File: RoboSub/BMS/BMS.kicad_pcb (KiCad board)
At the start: 2 copper layers, 72.2 x 72.2 mm, 36 parts, among them J1 CAN, J2 CAN, J3 DuraClik, J4 XT90, J5 XT90, J6 SWD_UART, J7 ExtPwrSw, K1 A3_Relay, Q1 PMV28ENEA, SW2 DBG2, SW3 DBG1, SW4 RST, U1 VXO7803, U2 TCAN330G, U3 STM32G0B1KxTxN, U4 CZ3AG7_HalEfSens

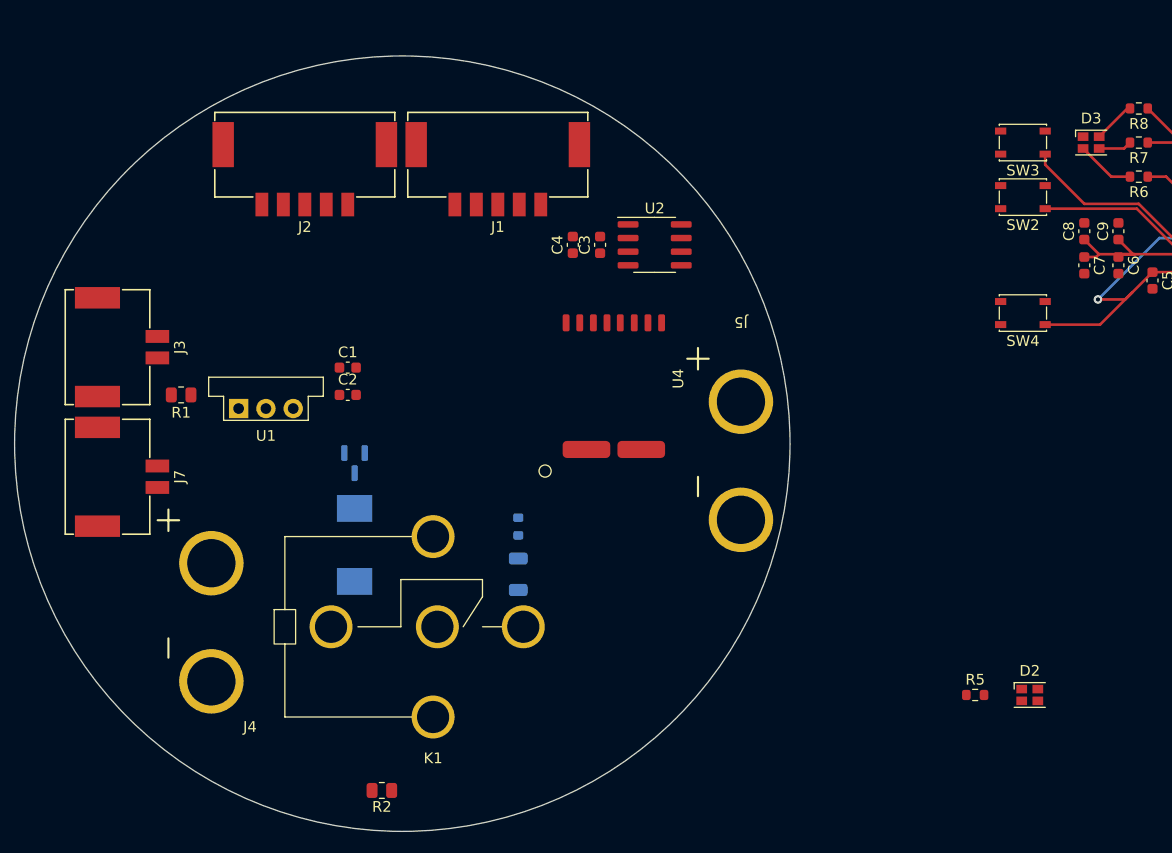
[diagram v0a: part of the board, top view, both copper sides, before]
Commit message: cleaned up schematic
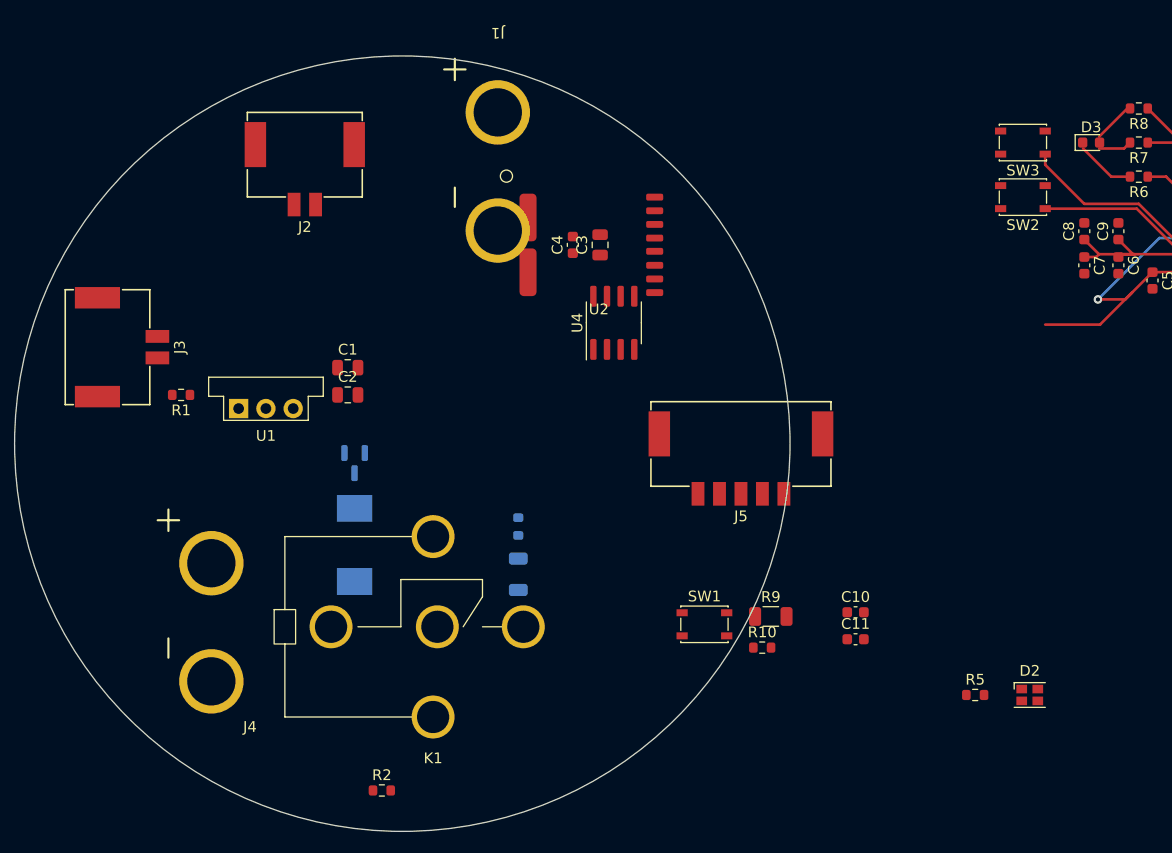
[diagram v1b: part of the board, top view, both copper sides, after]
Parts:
- removed J7: ExtPwrSw, extraparts:Molex_DuraClik_Vert_2pin
- removed SW4: RST, Button_Switch_SMD:SW_SPST_PTS810
- added C10: 100n, Capacitor_SMD:C_0603_1608Metric, F.Cu at (93.0, 68.5)
- added C11: 4.7u, Capacitor_SMD:C_0603_1608Metric, F.Cu at (93.0, 71.0)
- added R10: 120, Resistor_SMD:R_0603_1608Metric, F.Cu at (84.3, 71.8)
- added R9: 1k, Resistor_SMD:R_1206_3216Metric, F.Cu at (85.1, 68.9)
- added SW1: DBG2, Button_Switch_SMD:SW_SPST_PTS810, F.Cu at (78.9, 69.6)
- C1: value 4.7uF -> 10u; footprint Capacitor_SMD:C_0603_1608Metric -> Capacitor_SMD:C_0805_2012Metric
- C2: value 10uF -> 10u; footprint Capacitor_SMD:C_0603_1608Metric -> Capacitor_SMD:C_0805_2012Metric
- C3: value 100n -> 10u; footprint Capacitor_SMD:C_0603_1608Metric -> Capacitor_SMD:C_0805_2012Metric
- C4: value 4.7u -> 100n
- D2: value LED -> LED_ARGB
- D3: value LED_ARGB -> LED; footprint LED_SMD:LED_Cree-PLCC4_2x2mm_CW -> LED_SMD:LED_0603_1608Metric
- J1: value CAN -> battery; footprint extraparts:Molex_DuraClik_Vert_5pin -> BMS_Library:Conn_XT90
- J2: value CAN -> temp; footprint extraparts:Molex_DuraClik_Vert_5pin -> extraparts:Molex_DuraClik_Vert_2pin
- J3: value DuraClik -> ExtPwrSw
- J4: value XT90 -> output
- J5: value XT90 -> CAN; footprint BMS_Library:Conn_XT90 -> extraparts:Molex_DuraClik_Vert_5pin
- K1: value A3_Relay -> A31ASQ12VDC2R
- R1: footprint Resistor_SMD:R_0805_2012Metric -> Resistor_SMD:R_0603_1608Metric
- R2: value 10 -> 10k; footprint Resistor_SMD:R_0805_2012Metric -> Resistor_SMD:R_0603_1608Metric
- R3: value 4k -> 10
- R4: value 1k -> 100k
- R5: value 250 -> 10k
- SW2: value DBG2 -> DBG1
- SW3: value DBG1 -> RST
- U2: value TCAN330G -> CZ3A07; footprint Package_SO:SOIC-8_3.9x4.9mm_P1.27mm -> BMS_Library:CZ3AG7_HalEfSens
- U4: value CZ3AG7_HalEfSens -> TCAN330G; footprint BMS_Library:CZ3AG7_HalEfSens -> Package_SO:SOIC-8_3.9x4.9mm_P1.27mm
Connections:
- C1 pad 1: Net-(C1-Pad1) -> GND
- C1 pad 2: GND -> Net-(C1-Pad2)
- D2 pad 1: GND -> +3V3
- D2 pad 2: Net-(D2-Pad2) -> /R
- D2 pad 3: (no net) -> /G
- D2 pad 4: (no net) -> /B
- D3 pad 1: +3V3 -> GND
- D3 pad 2: /R -> Net-(D3-Pad2)
- J1 pad 1: Net-(J1-Pad1) -> GND
- J1 pad 2: Net-(J1-Pad2) -> +BATT
- J2 pad 1: Net-(J1-Pad1) -> GND
- J2 pad 2: Net-(J1-Pad2) -> /T_sense
- J3 pad 1: /T_sense -> Net-(C1-Pad2)
- J3 pad 2: GND -> +BATT
- J4 pad 1: +BATT -> GND
- J4 pad 2: GND -> VBUS
- J5 pad 1: /V_out -> VBUS
- J5 pad 2: GND -> /PCC_3V3
- K1 pad 85: Net-(D1-Pad2) -> +BATT
- K1 pad 86: Net-(D1-Pad1) -> Net-(D1-Pad2)
- K1 pad 87: /IP -> /VRAW
- Q1 pad 1: /MOSFET1 -> /enable
- Q1 pad 3: Net-(D1-Pad1) -> Net-(Q1-Pad3)
- R2 pad 1: +BATT -> GND
- R2 pad 2: Net-(D1-Pad2) -> /enable
- R3 pad 1: /V_sense -> Net-(Q1-Pad3)
- R3 pad 2: /IP -> Net-(D1-Pad2)
- R4 pad 1: /V_sense -> /VRAW
- R4 pad 2: GND -> /V_sense
- R5 pad 1: Net-(D2-Pad2) -> /V_sense
- R5 pad 2: /V_out -> GND
- SW2 pad 1: /DBG2 -> /DBG1
- SW3 pad 1: /DBG1 -> /RST
- U1 pad 1: Net-(C1-Pad1) -> Net-(C1-Pad2)
- U2 pad 1: /CAN_TX -> /VRAW
- U2 pad 5: unconnected-(U2-Pad5) -> VBUS
- U3 pad 11: /MOSFET1 -> /enable
- U4 pad 1: /IP -> /CAN_TX
- U4 pad 5: /V_out -> unconnected-(U4-Pad5)
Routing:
- net /RST: track 47.2 -> 64.4 mm
- net /DBG2: track 14.9 -> 0.00 mm
- net /R: track 3.96 -> 7.06 mm
- net /G: track 3.10 -> 0.00 mm
- net /DBG1: track 17.2 -> 14.9 mm

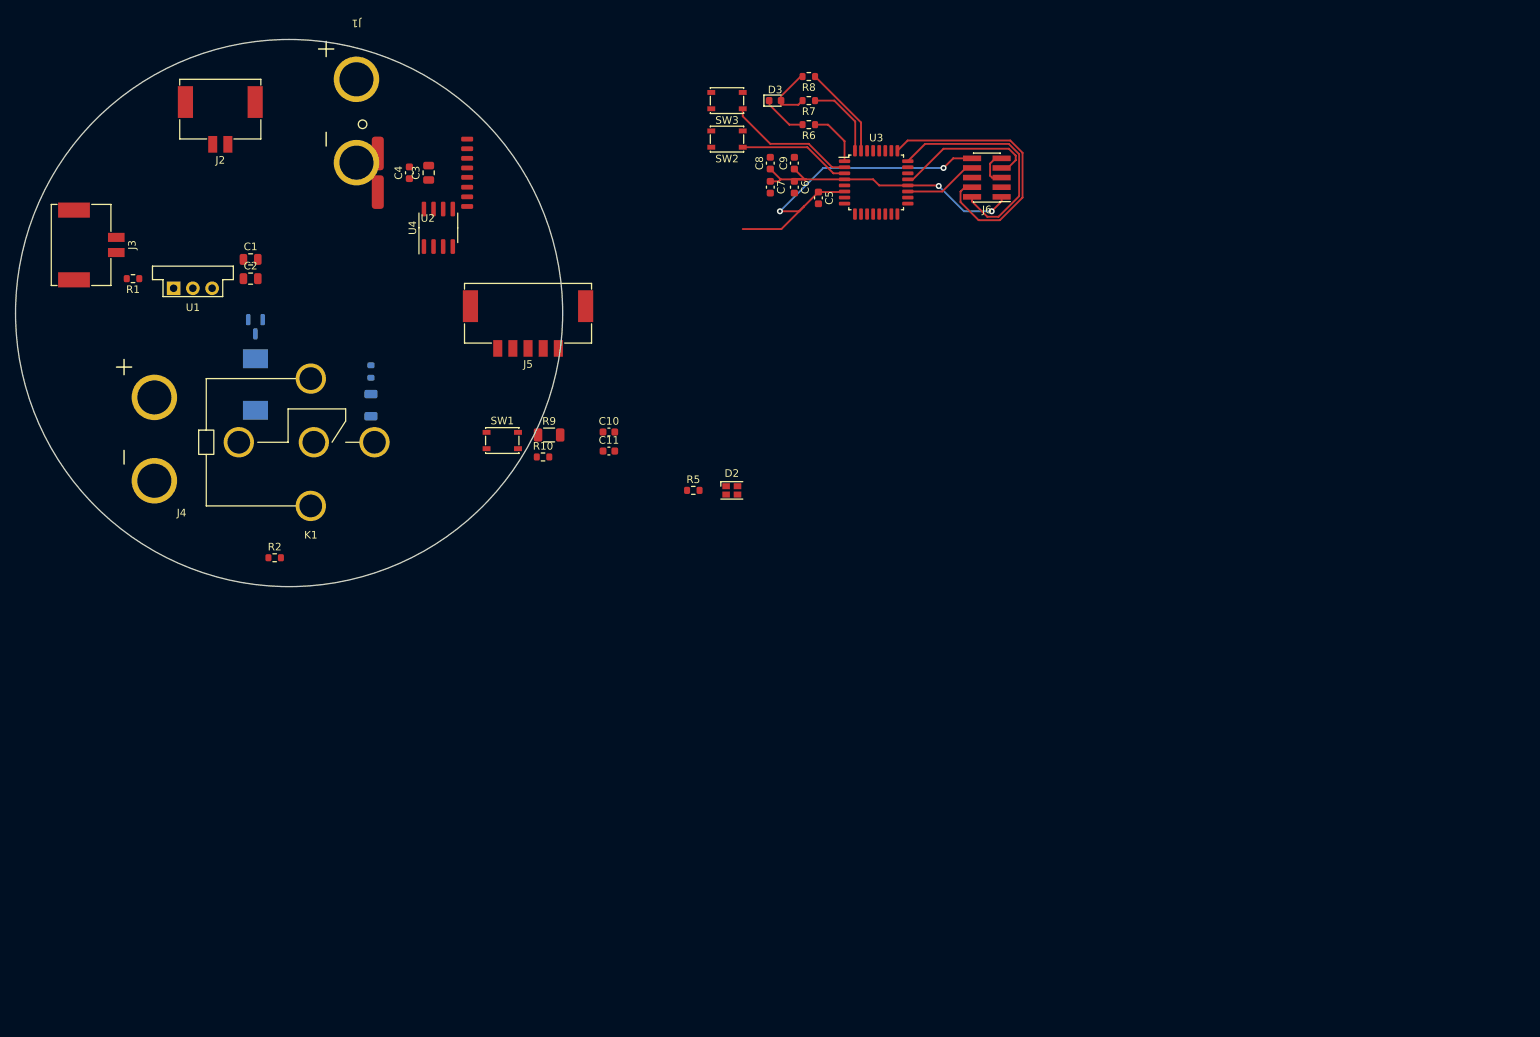
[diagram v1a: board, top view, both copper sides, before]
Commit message: PCC added to BMS. TODO: change TVS diode.
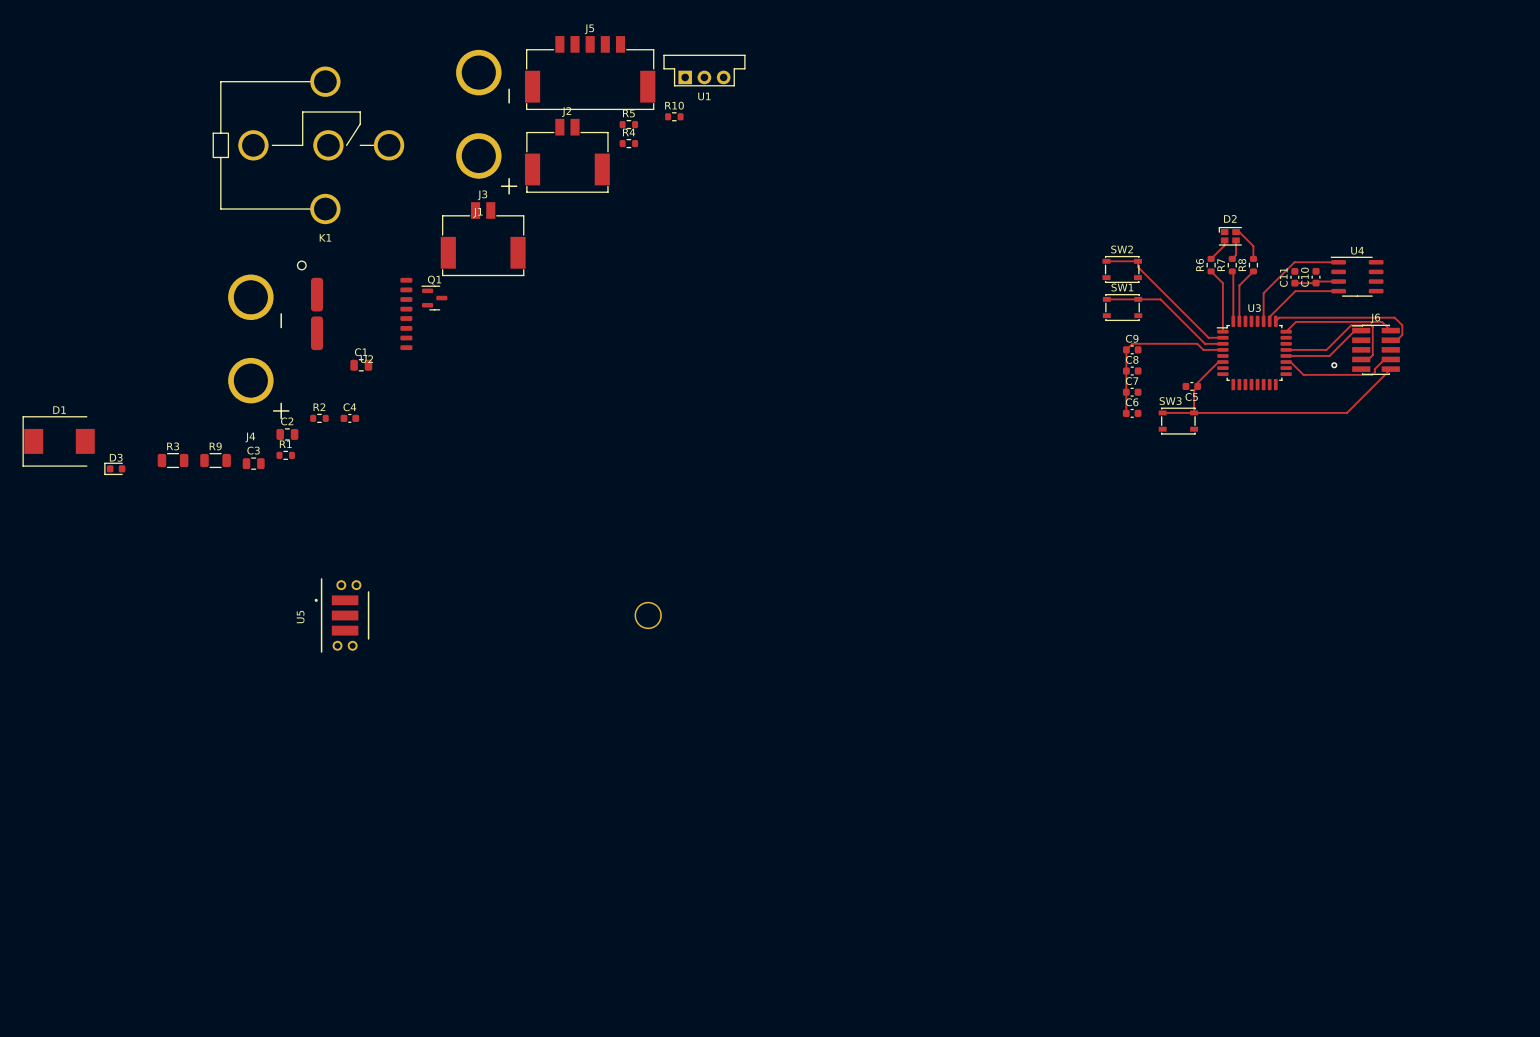
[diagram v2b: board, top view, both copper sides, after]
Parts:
- added U5: PCC, BMS_Library:PCC_footprint, F.Cu at (58.2, 92.7)
- D1: value TVS_Diode -> SMCJ13A_TVS; moved to F.Cu
- K1: value A31ASQ12VDC2R -> A31CSP12VDC2D
- Q1, R3, R4: moved to F.Cu
- moved U4 121.4 mm to (191.8, 48.0), turned to 0 degrees
- moved D3 99.6 mm to (28.0, 73.4)
- moved C10 95.5 mm to (186.3, 48.1), turned to 90 degrees
- moved C11 93.4 mm to (183.5, 48.1), turned to 90 degrees
- moved SW1 83.7 mm to (160.8, 52.1)
- moved D2 73.8 mm to (175.0, 42.7)
- moved SW3 73.0 mm to (168.1, 67.1), turned to 0 degrees
- moved U1 73.0 mm to (103.1, 21.7)
- moved R8 63.7 mm to (178.1, 46.5), turned to 90 degrees
- moved R7 60.0 mm to (175.3, 46.5), turned to 90 degrees
- moved J3 57.1 mm to (76.4, 47.8), turned to 0 degrees
- moved R6 56.2 mm to (172.5, 46.5), turned to 90 degrees
- moved J6 56.2 mm to (194.2, 57.7), turned to 0 degrees
- moved C5 55.2 mm to (169.9, 62.5), turned to 180 degrees
- moved C8 55.1 mm to (162.1, 60.5), turned to 0 degrees
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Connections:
- D1 pad 1: Net-(D1-Pad1) -> +BATT
- K1 pad 87a: (no net) -> unconnected-(K1-Pad87a)
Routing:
- net /RST: track 64.4 -> 41.1 mm, vias 2 -> 0
- net /DBG2: track 0.00 -> 17.7 mm
- net /NOGGIN/SWCLK: track 37.2 -> 20.4 mm
- net /NOGGIN/SWDIO: track 30.5 -> 14.8 mm
- net /CAN_TX: track 0.00 -> 15.3 mm
- net /CAN_RX: track 0.00 -> 11.1 mm
- net /NOGGIN/TX: track 9.77 -> 15.6 mm
- net /DBG1: track 14.9 -> 20.0 mm
- net GND: track 5.03 -> 0.00 mm
- net /LED_R: track 12.3 -> 7.35 mm
- net /LED_G: track 10.3 -> 6.64 mm
- net /G: track 0.00 -> 2.64 mm
- net /R: track 7.06 -> 4.75 mm
- net /B: track 5.46 -> 3.18 mm
- net /LED_B: track 7.44 -> 8.60 mm
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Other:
- board outline removed

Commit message: working on layout
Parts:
- U2: moved to B.Cu
- moved J4 166.1 mm to (207.0, 101.3), turned to 180 degrees
- moved J5 160.0 mm to (212.0, 130.0), turned to 90 degrees
- moved U2 133.9 mm to (189.8, 104.6), turned to -90 degrees
- moved U1 117.1 mm to (136.6, 133.9)
- moved K1 112.4 mm to (140.2, 104.6)
- moved U5 104.7 mm to (155.5, 131.3)
- moved J3 104.2 mm to (126.2, 139.3)
- moved J6 49.6 mm to (189.0, 107.0)
- moved C10 49.4 mm to (184.9, 97.4)
- moved C8 49.4 mm to (160.6, 109.8)
- moved D2 49.4 mm to (173.6, 92.0)
- moved SW3 49.4 mm to (166.7, 116.4)
- moved C5 49.4 mm to (168.5, 111.8)
- moved C7 49.4 mm to (160.6, 112.6)
- moved SW1 49.4 mm to (159.4, 101.4)
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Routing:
- net +3V3: track 38.9 -> 43.8 mm
- net /NOGGIN/RX: track 18.4 -> 14.5 mm
- net /NOGGIN/SWDIO: track 14.8 -> 11.0 mm
- net /NOGGIN/SWCLK: track 20.4 -> 16.6 mm
- net /RST: track 41.1 -> 37.3 mm
- net /NOGGIN/TX: track 15.6 -> 11.8 mm
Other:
- board outline added: 127 x 50.8 mm
